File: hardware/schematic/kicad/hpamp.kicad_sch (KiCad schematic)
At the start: 70 parts, among them J401 6.35mm, J402 3.5mm, K401 G6K-2F-Y 3VDC, Q401 2N7002, Q402 BC847, Q403 BC847, SW401 GAIN H/L, U401 OPA1612, U402 LME49600, U403 LME49600, U404 LME49600, U405 LME49600, U406 LM393

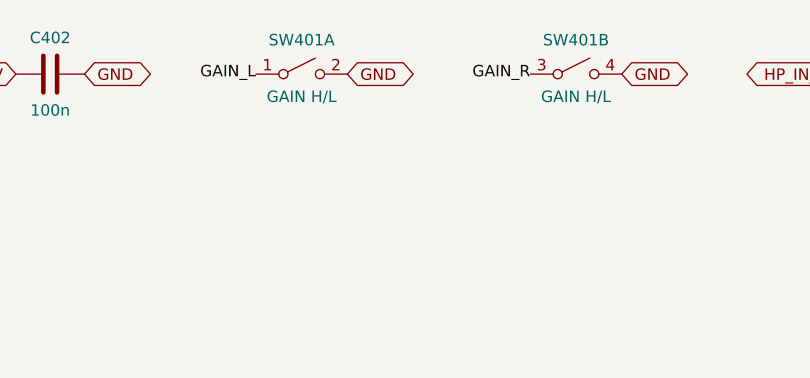
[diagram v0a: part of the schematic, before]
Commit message: Add footprints and starting PCB so Altium import resolves every part
Altium's ECO reported "Footprint Not Found" for every part (and the
resulting "Unknown Pin" / class-member errors) because only KiCad
footprint names were included. Now:

- aio.kicad_pcb: every part placed with its footprint, all pads on their
  nets (unrouted), generated by pcb.py
- aio.pretty/: the 45 footprints the design uses, bundled with the project
- footprint fixes: five names that did not exist in the KiCad library
  replaced (coupled inductors -> two SRR1260 per converter, SRP5030T,
  RK097 dual pot, NCJ6FI-H, DPDT gain switch); parts without an explicit
  footprint now keep the symbol's default; phantom switch moved from a
  momentary push-button to a latching slide switch
- check.py also verifies every PCB pad's net against design.py
- README: Altium import steps (full project, then Make PCB Library)

U203 (XU316) still has no footprint: its pin numbers are placeholders
until the official XMOS library part replaces it.
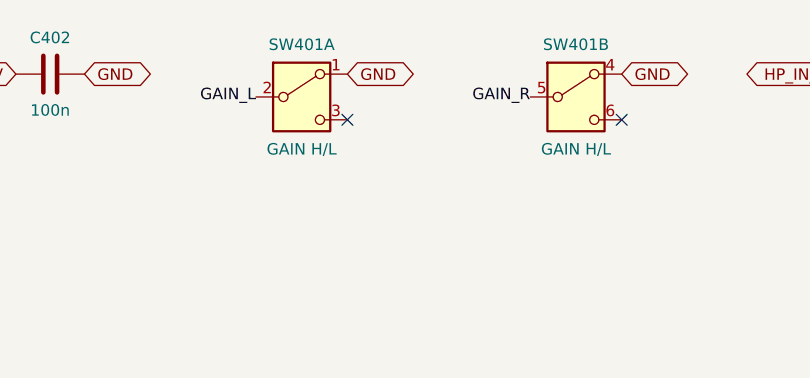
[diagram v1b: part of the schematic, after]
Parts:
- Q401, Q402, Q403: footprint (none) -> Package_TO_SOT_SMD:SOT-23
- SW401: footprint Button_Switch_THT:SW_Slide_SPDT_Straight_CK_OS102011MS2Q -> Button_Switch_SMD:SW_DPDT_CK_JS202011JCQN; symbol Switch:SW_DPST_x2 -> Switch:SW_DPDT_x2; MPN DPST slide/toggle -> JS202011JCQN
- U402, U403, U404, U405: footprint (none) -> Package_TO_SOT_SMD:TO-263-5_TabPin3
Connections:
- net GAIN_L: now also SW401.2 (B); no longer SW401.1 (A)
- net GAIN_R: now also SW401.5 (B); no longer SW401.3 (A)
- net GND: now also SW401.1 (A); no longer SW401.2 (B)
- no-connect marks 6 -> 8
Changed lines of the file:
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@@
   )
   (symbol
-    (lib_id "Switch:SW_DPST_x2")
-    (at 175.26 33.02 0)
+    (lib_id "Switch:SW_DPDT_x2")
+    (at 175.26 35.56 0)
     (unit 1)
     (in_bom yes)
@@
     (dnp no)
     (property "Reference" "SW401"
-      (at 175.26 29.24 0)
+      (at 175.26 29.75 0)
       (effects
         (font
@@
     )
     (property "Value" "GAIN H/L"
-      (at 175.26 35.53 0)
+      (at 175.26 41.37 0)
       (effects
         (font
@@
       )
     )
-    (property "Footprint" "Button_Switch_THT:SW_Slide_SPDT_Straight_CK_OS102011MS2Q"
-      (at 175.26 33.02 0)
+    (property "Footprint" "Button_Switch_SMD:SW_DPDT_CK_JS202011JCQN"
+      (at 175.26 35.56 0)
       (effects
         (font
@@
     )
     (property "Datasheet" ""
-      (at 175.26 33.02 0)
+      (at 175.26 35.56 0)
       (effects
         (font
@@
       )
     )
-    (property "MPN" "DPST slide/toggle"
-      (at 175.26 33.02 0)
+    (property "MPN" "JS202011JCQN"
+      (at 175.26 35.56 0)
       (effects
         (font
@@
     (pin "2"
     )
+    (pin "3"
+    )
     (instances
       (project "aio"
@@
     )
   )
-  (label "GAIN_L"
-    (at 170.18 33.02 180)
-    (fields_autoplaced)
-    (effects
-      (font
-        (size 1.27 1.27)
-      )
-      (justify right)
-    )
-  )
   (global_label "GND"
     (shape bidirectional)
@@
     )
   )
+  (label "GAIN_L"
+    (at 170.18 35.56 180)
+    (fields_autoplaced)
+    (effects
+      (font
+        (size 1.27 1.27)
+      )
+      (justify right)
+    )
+  )
+  (no_connect
+    (at 180.34 38.1)
+  )
   (symbol
-    (lib_id "Switch:SW_DPST_x2")
-    (at 205.74 33.02 0)
+    (lib_id "Switch:SW_DPDT_x2")
+    (at 205.74 35.56 0)
     (unit 2)
     (in_bom yes)
@@
     (dnp no)
     (property "Reference" "SW401"
-      (at 205.74 29.24 0)
+      (at 205.74 29.75 0)
       (effects
         (font
@@
     )
     (property "Value" "GAIN H/L"
-      (at 205.74 35.53 0)
+      (at 205.74 41.37 0)
       (effects
         (font
@@
       )
     )
-    (property "Footprint" "Button_Switch_THT:SW_Slide_SPDT_Straight_CK_OS102011MS2Q"
-      (at 205.74 33.02 0)
+    (property "Footprint" "Button_Switch_SMD:SW_DPDT_CK_JS202011JCQN"
+      (at 205.74 35.56 0)
       (effects
         (font
@@
     )
     (property "Datasheet" ""
-      (at 205.74 33.02 0)
+      (at 205.74 35.56 0)
       (effects
         (font
@@
       )
     )
-    (property "MPN" "DPST slide/toggle"
-      (at 205.74 33.02 0)
+    (property "MPN" "JS202011JCQN"
+      (at 205.74 35.56 0)
       (effects
         (font
@@
       )
     )
-    (pin "3"
-    )
     (pin "4"
     )
+    (pin "5"
+    )
+    (pin "6"
+    )
     (instances
       (project "aio"
@@
     )
   )
-  (label "GAIN_R"
-    (at 200.66 33.02 180)
-    (fields_autoplaced)
-    (effects
-      (font
-        (size 1.27 1.27)
-      )
-      (justify right)
-    )
-  )
   (global_label "GND"
     (shape bidirectional)
@@
     )
   )
+  (label "GAIN_R"
+    (at 200.66 35.56 180)
+    (fields_autoplaced)
+    (effects
+      (font
+        (size 1.27 1.27)
+      )
+      (justify right)
+    )
+  )
+  (no_connect
+    (at 210.82 38.1)
+  )
   (symbol
     (lib_id "Device:R")
@@
       )
     )
-    (property "Footprint" ""
+    (property "Footprint" "Package_TO_SOT_SMD:TO-263-5_TabPin3"
       (at 462.28 45.72 0)
       (effects
@@
       )
     )
-    (property "Footprint" ""
+    (property "Footprint" "Package_TO_SOT_SMD:TO-263-5_TabPin3"
       (at 63.5 88.9 0)
       (effects
@@
       )
     )
-    (property "Footprint" ""
+    (property "Footprint" "Package_TO_SOT_SMD:TO-263-5_TabPin3"
       (at 457.2 88.9 0)
       (effects
@@
       )
     )
-    (property "Footprint" ""
+    (property "Footprint" "Package_TO_SOT_SMD:TO-263-5_TabPin3"
       (at 63.5 132.08 0)
       (effects
@@
       )
     )
-    (property "Footprint" ""
+    (property "Footprint" "Package_TO_SOT_SMD:SOT-23"
       (at 358.14 132.08 0)
       (effects
@@
       )
     )
-    (property "Footprint" ""
+    (property "Footprint" "Package_TO_SOT_SMD:SOT-23"
       (at 411.48 172.72 0)
       (effects
@@
       )
     )
-    (property "Footprint" ""
+    (property "Footprint" "Package_TO_SOT_SMD:SOT-23"
       (at 457.2 172.72 0)
       (effects

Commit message: Split schematic into 14 A3 sheets, fix board outline, cluster placement
- Schematic: the five large A1/A0 sheets become 14 A3 sheets, one per
  function. Designators are unchanged (sections share one numbering
  sequence); the BOM is identical.
- PCB staging board: the outline was computed from board edges before any
  existed, so it came out far too small. It now encloses all parts. Parts
  are packed into one labelled cluster per sheet instead of one long strip.
- README: Altium steps for the "Missing child-sheet" errors (drop the top
  sheet, use global net scope) and layout guidance: don't autoroute the
  staging board.
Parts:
- removed C419: 10u, Capacitor_SMD:C_0805_2012Metric, symbol Device:C
- removed C420, C421: 100n, Capacitor_SMD:C_0603_1608Metric, symbol Device:C
- removed C422, C423: 47u 25V, Capacitor_SMD:CP_Elec_8x10, symbol Device:C_Polarized
- removed D401: 1N4148W, Diode_SMD:D_SOD-123, symbol Diode:1N4148W
- removed D402: BAT54, Diode_SMD:D_SOD-123, symbol Device:D_Schottky
- removed J401: 6.35mm, Connector_Audio:Jack_6.35mm_Neutrik_NMJ6HCD2_Horizontal, symbol Connector_Audio:AudioJack3
- removed J402: 3.5mm, Connector_Audio:Jack_3.5mm_CUI_SJ1-3533NG_Horizontal, symbol Connector_Audio:AudioJack3
- removed K401: G6K-2F-Y 3VDC, Relay_SMD:Relay_DPDT_Omron_G6K-2F-Y, symbol Relay:G6K-2
- removed Q401: 2N7002, Package_TO_SOT_SMD:SOT-23, symbol Transistor_FET:2N7002
- removed Q402, Q403: BC847, Package_TO_SOT_SMD:SOT-23, symbol Transistor_BJT:BC847
- removed R421: 1k, Resistor_SMD:R_0603_1608Metric, symbol Device:R
- removed R422: 220k, Resistor_SMD:R_0603_1608Metric, symbol Device:R
- removed R423, R425: 100k, Resistor_SMD:R_0603_1608Metric, symbol Device:R
- removed R424: 10.7k, Resistor_SMD:R_0603_1608Metric, symbol Device:R
- removed R426: 16.9k, Resistor_SMD:R_0603_1608Metric, symbol Device:R
- removed R427, R428, R431, R432: 10k, Resistor_SMD:R_0603_1608Metric, symbol Device:R
- removed R429, R430: 47k, Resistor_SMD:R_0603_1608Metric, symbol Device:R
- removed U406: LM393, Package_SO:SOIC-8_3.9x4.9mm_P1.27mm, symbol Comparator:LM393
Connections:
- no-connect marks 8 -> 6
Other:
- title: Headphone amplifier and protection -> Headphone amplifier
- moved on the sheet: C404, C405, C406, C407, C408, C409, C410, C411, C412, C413, C414, C415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
